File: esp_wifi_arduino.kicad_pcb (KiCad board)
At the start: 2 copper layers, 30 x 50 mm, 30 parts, among them CON1 AVR-ISP-6, IC1 ATMEGA328P-A, P1 CONN_15, P2 CONN_15, SW1 SW_PUSH, SW2 SW_PUSH, SW3 DIPSW4, U1 ADG3304, U2 ESP-WROOM-02, U3 NJM2391DL1-33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

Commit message: Circuit Create
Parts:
- removed CON1: AVR-ISP-6, pin_array_3x2
- added P3: CONN_1, M3_Drill, F.Cu at (77.0, 76.0)
- added P4: CONN_1, M3_Drill, F.Cu at (48.0, 76.0)
- moved D1 42.8 mm to (69.7, 35.9)
- moved R1 40.9 mm to (73.9, 35.9), turned to 180 degrees
- moved R2 22.9 mm to (73.9, 33.4)
- moved D2 21.4 mm to (69.7, 33.4), turned to 180 degrees
- moved C4 10.7 mm to (57.4, 45.6)
- moved P2 9.16 mm to (78.7, 63.5)
- moved C5 8.97 mm to (57.5, 36.0)
- moved P1 8.03 mm to (45.7, 38.1)
- moved C9 3.65 mm to (66.1, 62.5), turned to 90 degrees
- moved C10 2.33 mm to (67.3, 73.2), turned to 270 degrees
- moved C8 0.55 mm to (59.4, 60.3)
- moved X1 0.48 mm to (54.0, 39.9), turned to 90 degrees
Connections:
- U1 pad 12: /ArduinoRX33 -> /ArduinoTX33
- U1 pad 13: /ArduinoTX33 -> /ArduinoRX33
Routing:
- net GND: track 0.00 -> 393.0 mm, vias 0 -> 26
- net +3.3V: track 0.00 -> 86.1 mm, vias 0 -> 6
- net +5V: track 0.00 -> 84.4 mm, vias 0 -> 6
- net /D12: track 0.00 -> 65.9 mm, vias 0 -> 2
- net /RESET: track 0.00 -> 63.0 mm, vias 0 -> 6
- net /D11: track 0.00 -> 61.9 mm, vias 0 -> 2
- net /D10: track 0.00 -> 58.0 mm, vias 0 -> 2
- net /D9: track 0.00 -> 54.3 mm, vias 0 -> 2
- net /ArduinoRX33: track 0.00 -> 53.4 mm, vias 0 -> 2
- net /ArduinoTX33: track 0.00 -> 50.2 mm, vias 0 -> 2
- net /D13: track 0.00 -> 43.5 mm, vias 0 -> 4
- net /A0: track 0.00 -> 32.4 mm, vias 0 -> 1
- net /AREF: track 0.00 -> 32.2 mm, vias 0 -> 1
- net /A2: track 0.00 -> 30.3 mm, vias 0 -> 1
- net /A1: track 0.00 -> 29.9 mm, vias 0 -> 1
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- added copper zone on B.Cu, net GND
- added copper zone on F.Cu, net GND
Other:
- board size 30 x 50 mm -> 37 x 50 mm
- rule trace_min: 0.254 -> 0.127
- board text added: "+3.3V"
- board text added: "+5V"
- board text added: "A0"
- board text added: "A1"
- board text added: "A2"
- board text added: "A3"
- board text added: "A4"
- board text added: "A5"
- board text added: "A6"
- board text added: "A7"
- board text added: "AREF"
- board text added: "AVR RST"
- board text added: "Asumono-001-Rev.A"
- board text added: "Asumonoduino-Wifi"
- board text added: "D0"
- board text added: "D1"
- board text added: "D10"
- board text added: "D11"
- board text added: "D12"
- board text added: "D13"
- board text added: "D2"
- board text added: "D3"
- board text added: "D4"
- board text added: "D5"
- board text added: "D6"
- board text added: "D7"
- board text added: "D8"
- board text added: "D9"
- board text added: "EN"
- board text added: "ESP RST"
- board text added: "GND"
- board text added: "IO0"
- board text added: "IO15"
- board text added: "IO2"
- board text added: "PWR"
- board text added: "RST"

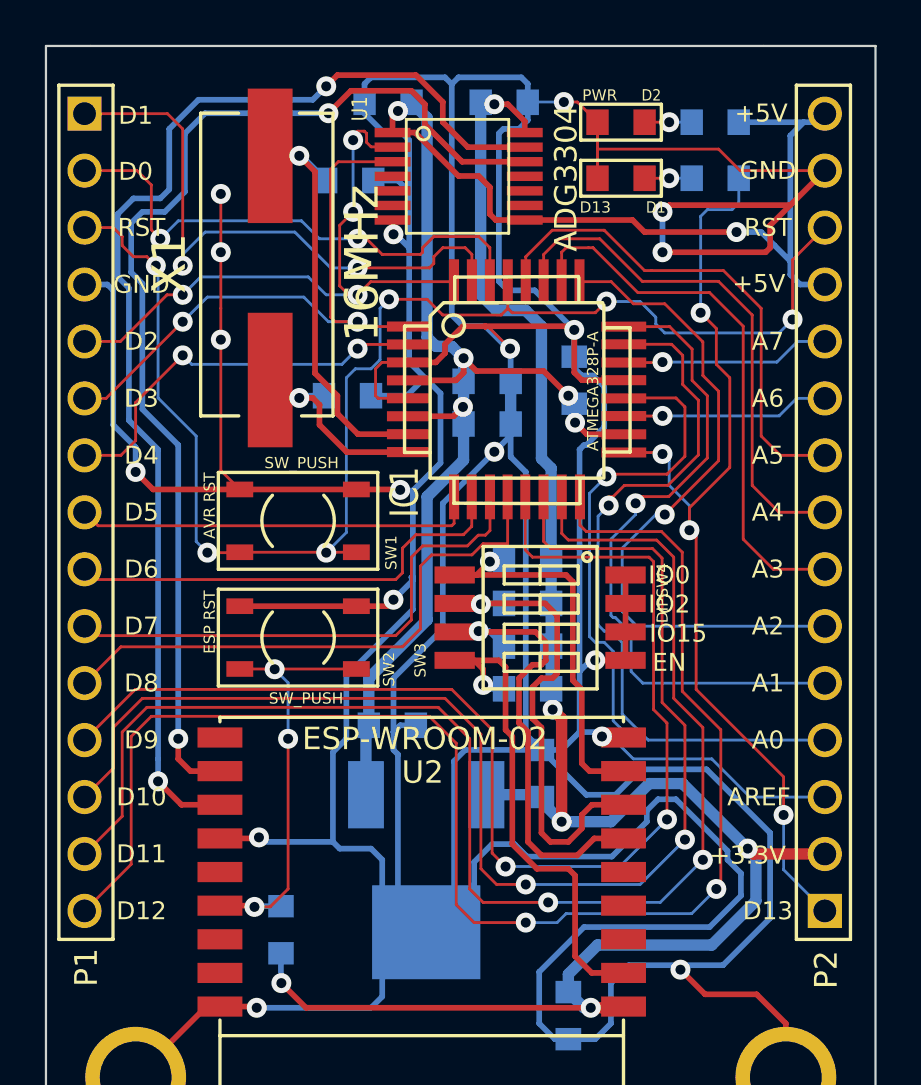
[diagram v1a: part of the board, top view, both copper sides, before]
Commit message: Fixed: FaceSilk
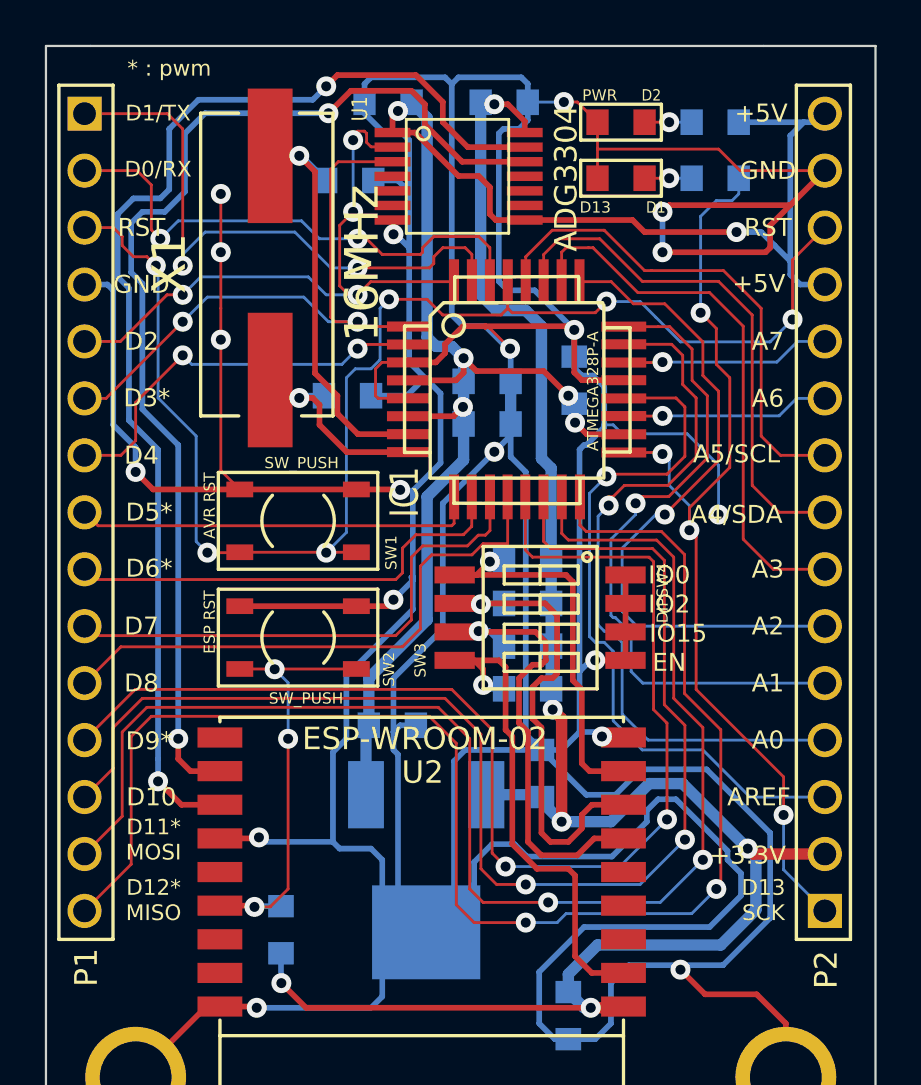
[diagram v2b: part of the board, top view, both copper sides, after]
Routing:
- net GND: track 393.0 -> 401.0 mm, vias 26 -> 27
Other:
- board text added: "* : pwm"
- board text added: "A4/SDA"
- board text added: "A5/SCL"
- board text added: "Asumono-K001-Rev.A"
- board text added: "D0/RX"
- board text added: "D1/TX"
- board text added: "D11* MOSI"
- board text added: "D12* MISO"
- board text added: "D13 SCK"
- board text added: "D3*"
- board text added: "D5*"
- board text added: "D6*"
- board text added: "D9*"
- board text removed: "A4"
- board text removed: "A5"
- board text removed: "Asumono-001-Rev.A"
- board text removed: "D0"
- board text removed: "D1"
- board text removed: "D11"
- board text removed: "D12"
- board text removed: "D3"
- board text removed: "D5"
- board text removed: "D6"
- board text removed: "D9"

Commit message: Rev.A
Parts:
- added G***: LOGO, LOGO, B.Cu at (75.2, 44.8)
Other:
- board text added: "D2(SS RX)"
- board text added: "D3(SS TX)"
- board text removed: "Asumono-K001-Rev.A"
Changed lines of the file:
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@@
     (area 33.571428 21.150002 92.714285 86.7)
     (thickness 1.6)
-    (drawings 53)
+    (drawings 58)
     (tracks 899)
     (zones 0)
-    (modules 31)
+    (modules 32)
     (nets 39)
   )
@@
   )
   (setup
-    (last_trace_width 0.127)
+    (last_trace_width 0.254)
     (user_trace_width 0.127)
     (user_trace_width 0.508)
@@
     (pad_to_mask_clearance 0)
     (aux_axis_origin 0 0)
-    (visible_elements 7FFF7FBF)
+    (visible_elements 7FFFFFBF)
     (pcbplotparams
-      (layerselection 3178497)
+      (layerselection 284196865)
       (usegerberextensions true)
       (excludeedgelayer true)
       (linewidth 0.150000)
       (plotframeref false)
-      (viasonmask false)
+      (viasonmask true)
       (mode 1)
       (useauxorigin false)
@@
       (psa4output false)
       (plotreference true)
-      (plotvalue true)
+      (plotvalue false)
       (plotothertext true)
       (plotinvisibletext false)
       (padsonsilk false)
-      (subtractmaskfromsilk false)
+      (subtractmaskfromsilk true)
       (outputformat 1)
       (mirror false)
-      (drillshape 1)
+      (drillshape 0)
       (scaleselection 1)
-      (outputdirectory ""))
+      (outputdirectory output/))
   )
   (net 0 "")
@@
   (module XTAL_HC-49   placed (layer F.Cu)
     (at 54 39.9 90)
-    (fp_text reference X1 (at 0.2 -4.5 90) (layer F.SilkS)
+    (fp_text reference X1 (at 0.2 0.1 90) (layer F.SilkS)
       (effects (font (size 1.5 1.5) (thickness 0.15)))
     )
@@
     )
   )
+  (module LOGO (layer B.Cu)
+    (at 75.2 44.8 90)
+    (fp_text reference G*** (at 0 -3.21564 90) (layer B.SilkS) hide
+      (effects (font (size 1.524 1.524) (thickness 0.3048)) (justify mirror))
+    )
+    (fp_text value LOGO (at 0 3.21564 90) (layer B.SilkS) hide
+      (effects (font (size 1.524 1.524) (thickness 0.3048)) (justify mirror))
+    )
+    (fp_poly (pts (xy 2.12852 -0.254) (xy 2.10058 0.42672) (xy 1.93294 1.02108) (xy 1.63576 1.524)
+      (xy 1.21412 1.92024) (xy 0.67564 2.19964) (xy 0.58166 2.23012) (xy 0.12192 2.34442)
+      (xy -0.28448 2.3495) (xy -0.71374 2.2479) (xy -0.762 2.23266) (xy -1.28016 1.9812)
+      (xy -1.71196 1.6129) (xy -1.96088 1.2954) (xy -2.10312 1.06426) (xy -2.19202 0.84836)
+      (xy -2.24282 0.5842) (xy -2.27076 0.22606) (xy -2.28346 -0.14478) (xy -2.26568 -0.35052)
+      (xy -2.2225 -0.3937) (xy -2.15392 -0.28194) (xy -2.09042 -0.07366) (xy -2.08026 -0.02286)
+      (xy -1.97358 0.45212) (xy -1.84404 0.82296) (xy -1.7018 1.06426) (xy -1.5875 1.15062)
+      (xy -1.39446 1.13284) (xy -1.22174 0.97282) (xy -1.09474 0.69596) (xy -1.0541 0.52324)
+      (xy -0.99822 0.23622) (xy -0.91948 -0.0889) (xy -0.89916 -0.16764) (xy -0.79756 -0.54864)
+      (xy -0.61214 0.2032) (xy -0.49784 0.62992) (xy -0.39878 0.91694) (xy -0.29972 1.08712)
+      (xy -0.18796 1.1684) (xy -0.0762 1.18618) (xy 0.10922 1.10236) (xy 0.26416 0.86106)
+      (xy 0.38608 0.46228) (xy 0.41148 0.34036) (xy 0.46736 0.07366) (xy 0.5334 -0.18034)
+      (xy 0.5969 -0.38354) (xy 0.6477 -0.50038) (xy 0.67056 -0.49276) (xy 0.70866 -0.24892)
+      (xy 0.77724 0.06604) (xy 0.8636 0.40386) (xy 0.9525 0.7112) (xy 1.03124 0.92964)
+      (xy 1.06172 0.99314) (xy 1.23444 1.17094) (xy 1.40462 1.18364) (xy 1.56718 1.0414)
+      (xy 1.7145 0.7493) (xy 1.8415 0.30988) (xy 1.86182 0.21336) (xy 1.94818 -0.16002)
+      (xy 2.0193 -0.38354) (xy 2.07772 -0.4572) (xy 2.11582 -0.37084) (xy 2.12852 -0.254)
+      (xy 2.12852 -0.254)) (layer B.SilkS) (width 0.00254))
+    (fp_poly (pts (xy 1.86182 -0.9017) (xy 1.80848 -0.7493) (xy 1.76784 -0.70104) (xy 1.70434 -0.57658)
+      (xy 1.62814 -0.33528) (xy 1.55702 -0.04318) (xy 1.47066 0.3429) (xy 1.39954 0.56388)
+      (xy 1.33858 0.6223) (xy 1.27254 0.51816) (xy 1.19888 0.25908) (xy 1.15316 0.06096)
+      (xy 1.016 -0.43434) (xy 0.8636 -0.76454) (xy 0.70358 -0.92456) (xy 0.54102 -0.91948)
+      (xy 0.381 -0.74676) (xy 0.23368 -0.4064) (xy 0.11684 0.0254) (xy 0.04318 0.3302)
+      (xy -0.0254 0.5588) (xy -0.0762 0.6731) (xy -0.08382 0.67818) (xy -0.127 0.60198)
+      (xy -0.1905 0.39878) (xy -0.26416 0.10668) (xy -0.28448 0.0127) (xy -0.40894 -0.4445)
+      (xy -0.55626 -0.75184) (xy -0.71628 -0.90678) (xy -0.88646 -0.9017) (xy -1.05664 -0.73914)
+      (xy -1.18872 -0.47752) (xy -1.30556 -0.0889) (xy -1.39446 0.36068) (xy -1.44272 0.56388)
+      (xy -1.50114 0.6731) (xy -1.51384 0.67818) (xy -1.5621 0.60198) (xy -1.62052 0.39878)
+      (xy -1.68148 0.11684) (xy -1.68656 0.09906) (xy -1.75768 -0.23622) (xy -1.8415 -0.5334)
+      (xy -1.91262 -0.71628) (xy -1.97612 -0.85852) (xy -1.9812 -0.97536) (xy -1.91516 -1.10998)
+      (xy -1.75768 -1.30302) (xy -1.6129 -1.46558) (xy -1.24968 -1.7526) (xy -0.78232 -1.9431)
+      (xy -0.26162 -2.03454) (xy 0.27178 -2.0193) (xy 0.7747 -1.8923) (xy 0.91948 -1.82626)
+      (xy 1.1938 -1.65608) (xy 1.46304 -1.43764) (xy 1.68656 -1.20904) (xy 1.83134 -1.00584)
+      (xy 1.86182 -0.9017) (xy 1.86182 -0.9017)) (layer B.SilkS) (width 0.00254))
+  )
+  (gr_line (start 44.6 47) (end 44.6 42) (angle 90) (layer B.SilkS) (width 0.2))
+  (gr_line (start 47 47) (end 44.6 47) (angle 90) (layer B.SilkS) (width 0.2))
+  (gr_line (start 47 42) (end 47 47) (angle 90) (layer B.SilkS) (width 0.2))
+  (gr_line (start 44.6 42) (end 47 42) (angle 90) (layer B.SilkS) (width 0.2))
+  (gr_text "D3(SS TX)" (at 50.5 45.7) (layer B.SilkS)
+    (effects (font (size 0.8 0.8) (thickness 0.2)) (justify mirror))
+  )
+  (gr_text "D2(SS RX)" (at 50.5 43.1) (layer B.SilkS)
+    (effects (font (size 0.8 0.8) (thickness 0.2)) (justify mirror))
+  )
   (gr_text "D13\nSCK" (at 76 68.1) (layer F.SilkS)
     (effects (font (size 0.7 0.7) (thickness 0.175)))
@@
     (effects (font (size 0.7 0.7) (thickness 0.175)))
   )
-  (gr_text Asumono-K001-Rev.A (at 63 76) (layer B.SilkS)
-    (effects (font (size 1.2 1.2) (thickness 0.2)) (justify mirror))
-  )
   (gr_text "AVR RST" (at 51.3 50.5 90) (layer F.SilkS)
     (effects (font (size 0.5 0.5) (thickness 0.1)))
@@
     (effects (font (size 0.5 0.5) (thickness 0.1)))
   )
-  (gr_text Asumonoduino-Wifi (at 75.8 52.3 90) (layer B.SilkS)
+  (gr_text Asumonoduino-Wifi (at 75.8 58.6 90) (layer B.SilkS)
     (effects (font (size 1.5 1.5) (thickness 0.3)) (justify mirror))
   )

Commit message: PCB Layout
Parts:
- removed D1: LED, HANDSOL_0603
- removed G***: LOGO, LOGO
- removed P3, P4: CONN_1, M3_Drill
- removed R1: R, HANDSOL_0603
- added P5: CONN_01X04, PIN_ARRAY_4x1, F.Cu at (94.0, 102.9)
- added P6: CONN_01X04, PIN_ARRAY_4x1, F.Cu at (129.5, 102.9)
- added S1: RX_SEL, SEL, B.Cu at (99.0, 74.0)
- added S2: TX_SEL, SEL, B.Cu at (99.0, 81.0)
- added S3: EN_SEL, ALPS_SSSS213202(SlideSW), F.Cu at (119.0, 65.5)
- C4, C5, R2: moved to F.Cu
- P1, P2: value CONN_15 -> CONN_01X15
- U1: moved to B.Cu
- moved C7 77.2 mm to (111.0, 94.0)
- moved SW2 71.2 mm to (124.0, 75.0), turned to 90 degrees
- moved C6 70.9 mm to (111.0, 81.0), turned to 0 degrees
- moved C8 70.7 mm to (124.0, 89.0)
- moved C9 69.5 mm to (124.0, 101.0), turned to 0 degrees
- moved U1 69.3 mm to (108.0, 88.0), turned to 180 degrees
- moved SW1 67.1 mm to (118.0, 75.0), turned to 90 degrees
- moved C10 64.3 mm to (124.0, 103.5), turned to 0 degrees
- moved U3 64.3 mm to (119.0, 95.0), turned to 270 degrees
- moved SW3 63.3 mm to (121.0, 85.0), turned to 90 degrees
- moved D2 62.5 mm to (125.0, 62.5), turned to 90 degrees
- moved R5 62.5 mm to (121.0, 85.5), turned to 0 degrees
- moved R6 62.2 mm to (121.0, 83.0), turned to 0 degrees
- moved R7 61.9 mm to (121.0, 80.5), turned to 0 degrees
- moved R2 61.4 mm to (125.0, 67.5), turned to 90 degrees
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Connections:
- U1 pad 1: +5V -> +3.3V
- U1 pad 12: /ArduinoTX33 -> N-0000027
- U1 pad 13: /ArduinoRX33 -> N-0000026
- U1 pad 14: +3.3V -> +5V
- U1 pad 2: /D2 -> /ESP_TX
- U1 pad 3: /D3 -> /ESP_RX
- U1 pad 8: +5V -> N-0000011
- U2 pad 10: (no net) -> /IO4
- U2 pad 11: /ArduinoTX33 -> /ESP_RX
- U2 pad 12: /ArduinoRX33 -> /ESP_TX
- U2 pad 14: (no net) -> /IO5
- U2 pad 17: (no net) -> /IO16
- U2 pad 3: (no net) -> /IO14
- U2 pad 4: (no net) -> /IO12
- U2 pad 5: (no net) -> /IO13
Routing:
- net GND: track 401.0 -> 0.00 mm, vias 27 -> 0
- net +3.3V: track 86.4 -> 0.00 mm, vias 6 -> 0
- net +5V: track 84.4 -> 0.00 mm, vias 6 -> 0
- net /D12: track 65.9 -> 0.00 mm, vias 2 -> 0
- net /RESET: track 63.2 -> 0.00 mm, vias 6 -> 0
- net /D11: track 61.9 -> 0.00 mm, vias 2 -> 0
- net /D10: track 58.0 -> 0.00 mm, vias 2 -> 0
- net /D9: track 54.3 -> 0.00 mm, vias 2 -> 0
- net /ArduinoRX33: track 53.4 -> 0.00 mm, vias 2 -> 0
- net /ArduinoTX33: track 50.2 -> 0.00 mm, vias 2 -> 0
- net /D13: track 43.2 -> 0.00 mm, vias 4 -> 0
- net /A0: track 32.3 -> 0.00 mm, vias 1 -> 0
- net /AREF: track 31.7 -> 0.00 mm, vias 1 -> 0
- net /A2: track 30.3 -> 0.00 mm, vias 1 -> 0
- net /A1: track 29.9 -> 0.00 mm, vias 1 -> 0
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- removed copper zone on B.Cu, net GND
- removed copper zone on F.Cu, net GND
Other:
- board size 37 x 50 mm -> 40 x 50 mm
- rule trace_min: 0.127 -> 0.254
- board text removed: "* : pwm"
- board text removed: "+3.3V"
- board text removed: "+5V"
- board text removed: "A0"
- board text removed: "A1"
- board text removed: "A2"
- board text removed: "A3"
- board text removed: "A4/SDA"
- board text removed: "A5/SCL"
- board text removed: "A6"
- board text removed: "A7"
- board text removed: "AREF"
- board text removed: "AVR RST"
- board text removed: "Asumonoduino-Wifi"
- board text removed: "D0/RX"
- board text removed: "D1/TX"
- board text removed: "D10"
- board text removed: "D11* MOSI"
- board text removed: "D12* MISO"
- board text removed: "D13"
- board text removed: "D13 SCK"
- board text removed: "D2"
- board text removed: "D2(SS RX)"
- board text removed: "D3(SS TX)"
- board text removed: "D3*"
- board text removed: "D4"
- board text removed: "D5*"
- board text removed: "D6*"
- board text removed: "D7"
- board text removed: "D8"
- board text removed: "D9*"
- board text removed: "EN"
- board text removed: "ESP RST"
- board text removed: "GND"
- board text removed: "IO0"
- board text removed: "IO15"
- board text removed: "IO2"
- board text removed: "PWR"
- board text removed: "RST"

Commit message: Draw Pattern
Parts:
- removed S3: EN_SEL, ALPS_SSSS213202(SlideSW)
- added SW4: SWITCH_INV, ALPS_SSSS213202(SlideSW), F.Cu at (119.1, 65.1)
- C4, C5: moved to B.Cu
- moved P5 35.6 mm to (129.5, 102.9)
- moved P6 35.6 mm to (94.0, 102.9), turned to 270 degrees
- moved C8 12.8 mm to (125.8, 101.7)
- moved C9 10.9 mm to (113.1, 101.7), turned to 180 degrees
- moved R5 8.63 mm to (122.5, 77.0), turned to 270 degrees
- moved R6 6.08 mm to (120.0, 77.0), turned to 270 degrees
- moved C5 5.84 mm to (102.2, 67.3), turned to 180 degrees
- moved C4 5.74 mm to (107.7, 67.3), turned to 0 degrees
- moved R7 4.95 mm to (117.5, 77.0), turned to 270 degrees
- moved R3 4.12 mm to (125.0, 77.0), turned to 270 degrees
- moved U3 2.77 mm to (119.6, 97.7), turned to 180 degrees
- moved C10 1.70 mm to (123.2, 105.0)
- moved S1 1.68 mm to (98.5, 72.4)
- moved C7 1.00 mm to (111.0, 95.0)
- moved R4 1.00 mm to (107.0, 97.5)
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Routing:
- net GND: track 0.00 -> 260.4 mm, vias 0 -> 40
- net +5V: track 0.00 -> 108.8 mm, vias 0 -> 5
- net +3.3V: track 0.00 -> 74.7 mm, vias 0 -> 4
- net N-0000015: track 0.00 -> 53.8 mm, vias 0 -> 6
- net /RESET: track 0.00 -> 53.3 mm, vias 0 -> 3
- net /IO4: track 0.00 -> 43.3 mm, vias 0 -> 4
- net N-0000011: track 0.00 -> 43.2 mm, vias 0 -> 3
- net /IO5: track 0.00 -> 38.2 mm, vias 0 -> 1
- net /D0: track 0.00 -> 37.4 mm, vias 0 -> 2
- net /D1: track 0.00 -> 35.0 mm, vias 0 -> 1
- net N-0000044: track 0.00 -> 34.3 mm, vias 0 -> 2
- net /D13: track 0.00 -> 31.5 mm
- net /A6: track 0.00 -> 31.3 mm, vias 0 -> 1
- net /A7: track 0.00 -> 30.1 mm, vias 0 -> 1
- net /ESP_TX: track 0.00 -> 29.7 mm, vias 0 -> 1
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- added copper zone on B.Cu, net GND
- added copper zone on F.Cu, net GND
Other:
- net class Power added: clearance 0.254, trace_width 0.508, via_dia 0.889, via_drill 0.635

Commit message: Create Production File
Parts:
- added G***: LOGO, LOGO, B.Cu at (124.5, 63.4)
- added G***: LOGO, LOGO, F.Cu at (99.1, 105.6)
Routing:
- net GND: track 260.4 -> 316.0 mm, vias 40 -> 46
- net N-0000045: track 28.7 -> 30.3 mm
- net N-0000044: track 34.3 -> 35.1 mm
- net N-0000046: track 25.9 -> 26.6 mm
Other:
- board text added: "+3V3"
- board text added: "+5V"
- board text added: "A0"
- board text added: "A1"
- board text added: "A2"
- board text added: "A3"
- board text added: "A4 SDA"
- board text added: "A5 SCL"
- board text added: "A6"
- board text added: "A7"
- board text added: "AREF"
- board text added: "AVR"
- board text added: "Asumonoduino"
- board text added: "BootMode"
- board text added: "D0"
- board text added: "D0 RX"
- board text added: "D1"
- board text added: "D1 TX"
- board text added: "D10"
- board text added: "D11"
- board text added: "D12"
- board text added: "D13"
- board text added: "D2"
- board text added: "D2 SRX"
- board text added: "D3"
- board text added: "D3 STX"
- board text added: "D4"
- board text added: "D5"
- board text added: "D6"
- board text added: "D7"
- board text added: "D8"
- board text added: "D9"
- board text added: "EN"
- board text added: "GND"
- board text added: "Hi-Z"
- board text added: "IO0"
- board text added: "IO12"
- board text added: "IO13"
- board text added: "IO14"
- board text added: "IO15"
- board text added: "IO16"
- board text added: "IO2"
- board text added: "IO4"
- board text added: "IO5"
- board text added: "PWR"
- board text added: "RST"
- board text added: "RX"
- board text added: "Rev.B"
- board text added: "TX"
- board text added: "UART"
- board text added: "UART Pin Mapping"
- board text added: "Wifi"
- board text added: "Wifi x Arduino"

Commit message: Update Pattern
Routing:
- net GND: track 316.0 -> 326.3 mm, vias 46 -> 48
- net N-0000026: track 24.0 -> 25.9 mm
- net (no net): track 1.54 -> 0.00 mm, vias 1 -> 0
- net N-0000043: track 24.5 -> 23.4 mm
- net /D13: track 31.5 -> 30.5 mm
